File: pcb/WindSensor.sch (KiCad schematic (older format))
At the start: 21 parts, among them P1 SP, P10 3v3, P11 GND, P12 SDA, P13 SCL, P2 0V, P3 3v3, P4 SP, P5 SDA, P6 SCL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

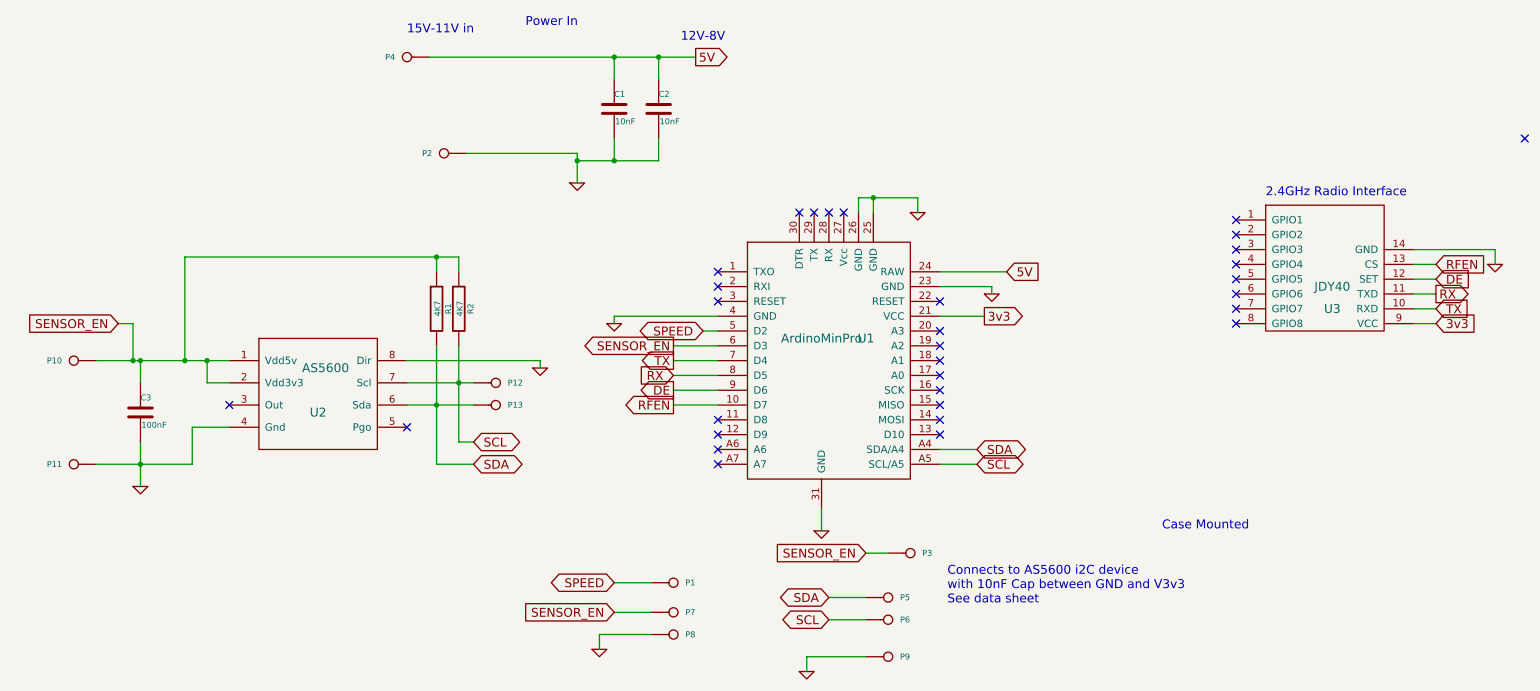
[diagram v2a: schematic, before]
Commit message: Fixed missing windspeed ouptput
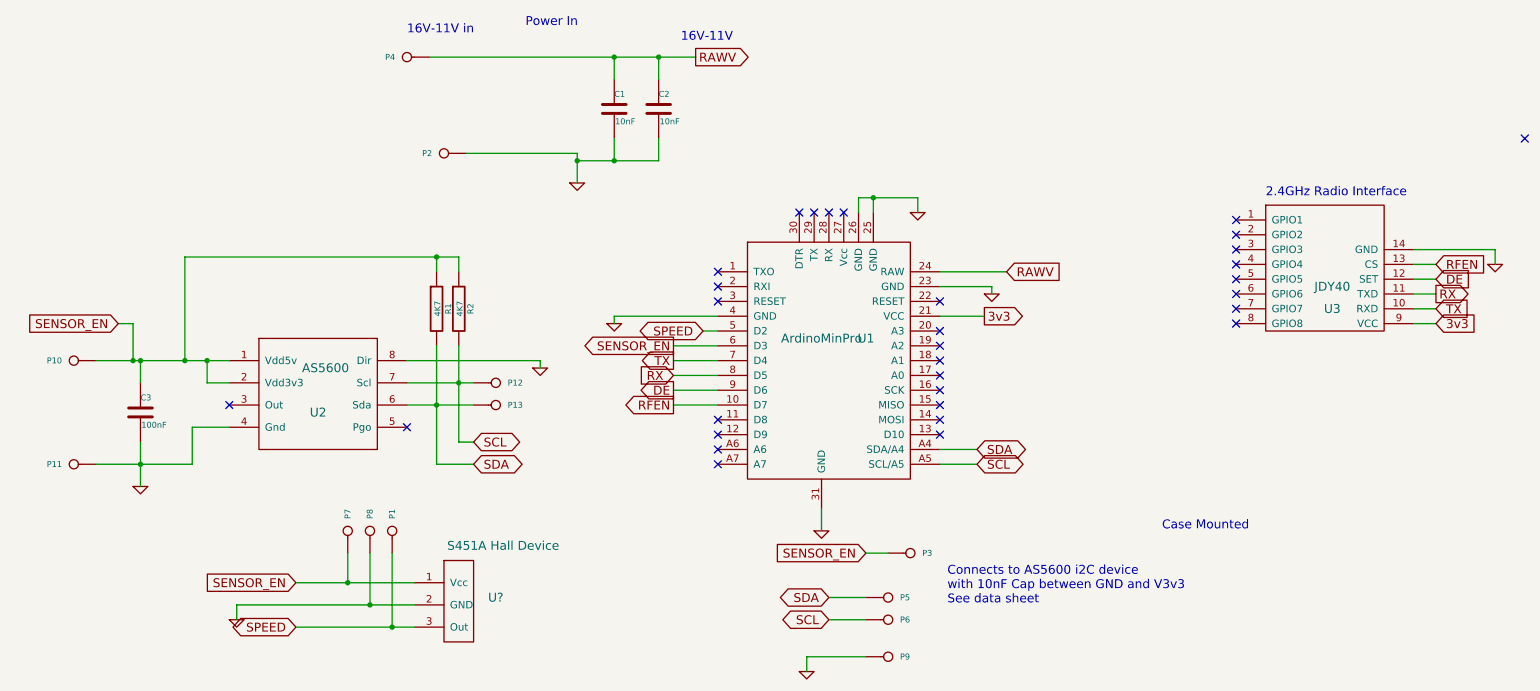
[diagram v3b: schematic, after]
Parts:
- added U?: S451A Hall Device, symbol 3144
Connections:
- net GND: now also U?.2 (GND)
- net SENSOR_EN: now also U?.1 (Vcc)
- net SPEED: now also U?.3 (Out)
- net 5V renamed RAWV
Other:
- note added: "16V-11V"
- note added: "16V-11V in"
- note removed: "12V-8V"
- note removed: "15V-11V in"
- moved on the sheet: P1, P7, P8
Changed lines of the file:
@@
 	1    0    0    -1
 $EndComp
-Text GLabel 4300 5450 0    60   BiDi ~ 0
+Text GLabel 2150 5750 0    60   BiDi ~ 0
 SPEED
 $Comp
@@
 DE
 Text GLabel 6950 3350 2    60   Input ~ 0
-5V
+RAWV
 Text Notes 8000 5100 0    60   ~ 0
 Case Mounted
@@
 Power In
 Text GLabel 4850 1900 2    60   Output ~ 0
-5V
+RAWV
 Text Notes 2900 1750 0    60   ~ 0
-15V-11V in
+16V-11V in
 Text Notes 4750 1800 0    60   ~ 0
-12V-8V
+16V-11V
 $Comp
 L GND #PWR05
@@
 L CONN_1 P1
 U 1 1 5FCE5DF1
-P 4700 5450
-F 0 "P1" H 4780 5450 40  0000 L CNN
-F 1 "SP" H 4700 5505 30  0001 C CNN
-F 2 "Pin_Headers:Pin_Header_Straight_1x01_Pitch2.54mm_SMD_Pin1Left" H 4700 5450 60  0001 C CNN
-F 3 "" H 4700 5450 60  0001 C CNN
-	1    4700 5450
-	1    0    0    -1
+P 2800 5100
+F 0 "P1" H 2880 5100 40  0000 L CNN
+F 1 "SP" H 2800 5155 30  0001 C CNN
+F 2 "Pin_Headers:Pin_Header_Straight_1x01_Pitch2.54mm_SMD_Pin1Left" H 2800 5100 60  0001 C CNN
+F 3 "" H 2800 5100 60  0001 C CNN
+	1    2800 5100
+	0    -1   -1   0
 $EndComp
 $Comp
@@
 L CONN_1 P7
 U 1 1 5FCF3E5D
-P 4700 5650
-F 0 "P7" H 4780 5650 40  0000 L CNN
-F 1 "5V" H 4700 5705 30  0001 C CNN
-F 2 "Pin_Headers:Pin_Header_Straight_1x01_Pitch2.54mm_SMD_Pin1Left" H 4700 5650 60  0001 C CNN
-F 3 "" H 4700 5650 60  0001 C CNN
-	1    4700 5650
-	1    0    0    -1
+P 2500 5100
+F 0 "P7" H 2580 5100 40  0000 L CNN
+F 1 "5V" H 2500 5155 30  0001 C CNN
+F 2 "Pin_Headers:Pin_Header_Straight_1x01_Pitch2.54mm_SMD_Pin1Left" H 2500 5100 60  0001 C CNN
+F 3 "" H 2500 5100 60  0001 C CNN
+	1    2500 5100
+	0    -1   -1   0
 $EndComp
 $Comp
 L GND #PWR08
 U 1 1 5FCF3F31
-P 4200 5900
-F 0 "#PWR08" H 4200 5900 30  0001 C CNN
-F 1 "GND" H 4200 5830 30  0001 C CNN
-F 2 "" H 4200 5900 60  0001 C CNN
-F 3 "" H 4200 5900 60  0001 C CNN
-	1    4200 5900
+P 1750 5700
+F 0 "#PWR08" H 1750 5700 30  0001 C CNN
+F 1 "GND" H 1750 5630 30  0001 C CNN
+F 2 "" H 1750 5700 60  0001 C CNN
+F 3 "" H 1750 5700 60  0001 C CNN
+	1    1750 5700
 	1    0    0    -1
 $EndComp
@@
 L CONN_1 P8
 U 1 1 5FCF3F60
-P 4700 5800
-F 0 "P8" H 4780 5800 40  0000 L CNN
-F 1 "GND" H 4700 5855 30  0001 C CNN
-F 2 "Pin_Headers:Pin_Header_Straight_1x01_Pitch2.54mm_SMD_Pin1Left" H 4700 5800 60  0001 C CNN
-F 3 "" H 4700 5800 60  0001 C CNN
-	1    4700 5800
-	1    0    0    -1
+P 2650 5100
+F 0 "P8" H 2730 5100 40  0000 L CNN
+F 1 "GND" H 2650 5155 30  0001 C CNN
+F 2 "Pin_Headers:Pin_Header_Straight_1x01_Pitch2.54mm_SMD_Pin1Left" H 2650 5100 60  0001 C CNN
+F 3 "" H 2650 5100 60  0001 C CNN
+	1    2650 5100
+	0    -1   -1   0
 $EndComp
 NoConn ~ 5000 3450
@@
 	5700 4950 5700 5100
 Wire Wire Line
-	4300 5450 4550 5450
+	2150 5750 2950 5750
 Wire Wire Line
 	4700 4150 5000 4150
@@
 	5600 5950 6000 5950
 Wire Wire Line
-	4300 5650 4550 5650
-Wire Wire Line
-	4550 5800 4200 5800
-Wire Wire Line
-	4200 5800 4200 5900
+	2150 5450 2950 5450
+Wire Wire Line
+	1750 5600 2950 5600
+Wire Wire Line
+	1750 5600 1750 5700
 Wire Wire Line
 	5000 4050 4700 4050
@@
 	1700 4400 1450 4400
 Wire Wire Line
-	1450 4650 1450 4400
-Wire Wire Line
-	800  4650 1450 4650
+	1450 4400 1450 4650
+Wire Wire Line
+	1450 4650 800  4650
 Wire Wire Line
 	1100 4500 1100 4800
@@
 Wire Wire Line
 	5000 4250 4700 4250
-Text GLabel 4300 5650 0    60   Input ~ 0
+Text GLabel 2150 5450 0    60   Input ~ 0
 SENSOR_EN
+$Comp
+L 3144 U?
+U 1 1 603DF19B
+P 3450 5750
+F 0 "U?" H 3500 5950 60  0000 C CNN
+F 1 "S451A Hall Device" H 3550 6300 60  0000 C CNN
+F 2 "" H 3450 5750 60  0001 C CNN
+F 3 "" H 3450 5750 60  0001 C CNN
+	1    3450 5750
+	1    0    0    -1
+$EndComp
+Wire Wire Line
+	2800 5250 2800 5750
+Connection ~ 2800 5750
+Wire Wire Line
+	2650 5250 2650 5600
+Connection ~ 2650 5600
+Wire Wire Line
+	2500 5250 2500 5450
+Connection ~ 2500 5450
 $EndSCHEMATC
